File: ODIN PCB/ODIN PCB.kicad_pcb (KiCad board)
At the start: 2 copper layers, 67.6 x 56.4 mm, 18 parts, among them P2 POWER, SW1 BATTEST

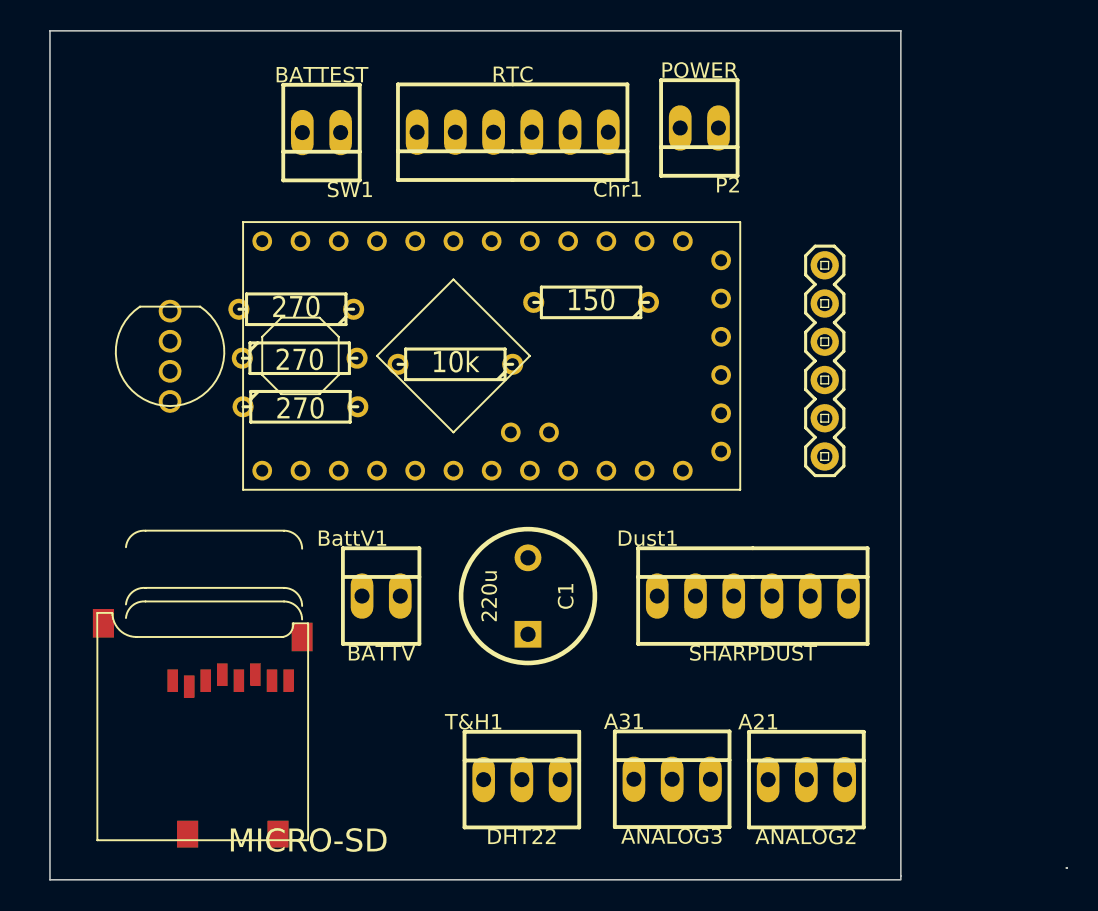
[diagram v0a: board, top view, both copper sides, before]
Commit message: Next iteration. Better net labelling. From Sam's message: "I've got it down to about 40mm x 56 mm.   Probably needs checking for connectivity issues and errors.   It passed the KiCad design rules check.   If we want to hang the SD card off the edge of the top surface the pin orientation does not need to be changed but I'd need to move the footprint to the left to avoid an overlap with the battery test header.   I haven't done anything with the silkscreen labels yet"
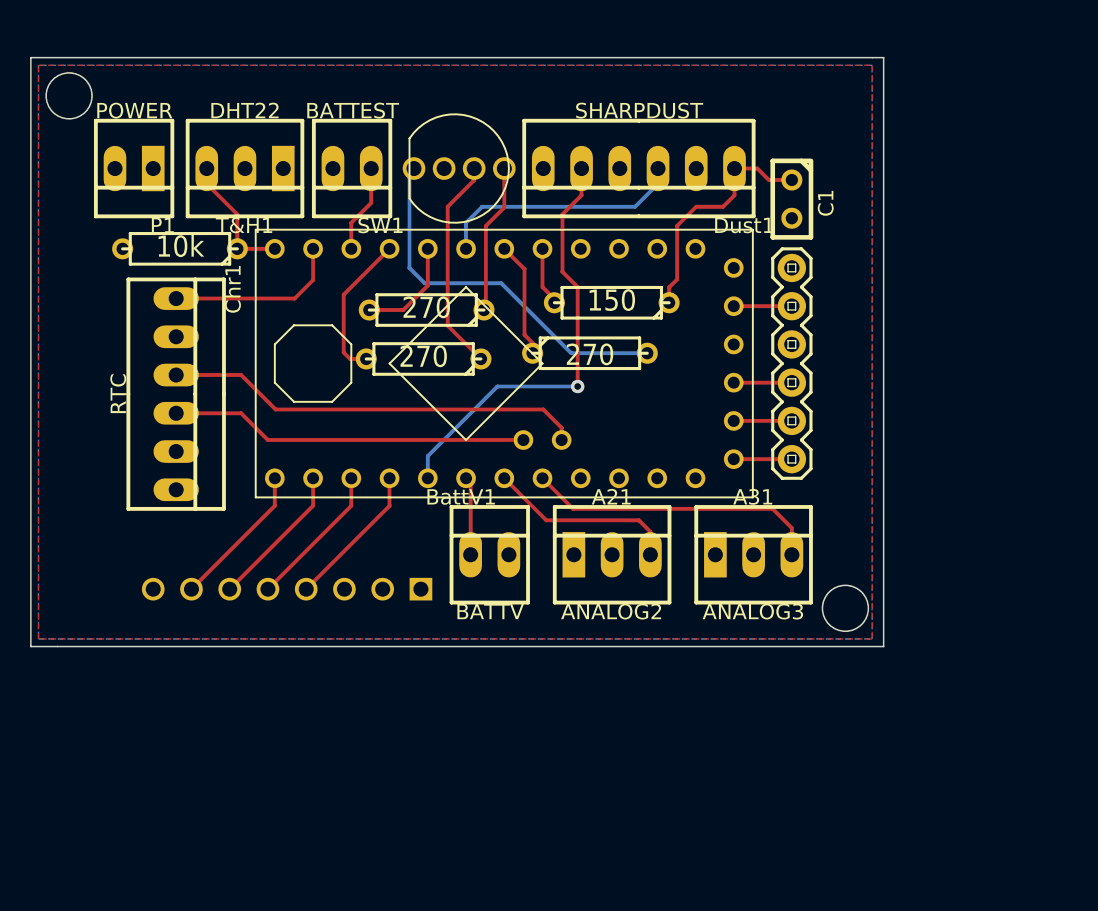
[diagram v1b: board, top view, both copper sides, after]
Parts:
- removed P2: POWER, PINHEAD1-2
- added P1: POWER, conn2pwr, F.Cu at (126.2, 106.9)
- A21, A31, T&H1: footprint PINHEAD1-3 -> header3
- C1: footprint C2V8 -> C1
- GUS1: value 5MMRGBLED -> 5mmRGB
- SD1: footprint adafruit-MICROSD -> microSD; moved to B.Cu
- moved T&H1 44.6 mm to (133.6, 106.9), turned to 180 degrees
- moved C1 31.7 mm to (169.9, 109.0), turned to 270 degrees
- moved Dust1 29.4 mm to (159.8, 106.9), turned to 180 degrees
- moved Chr1 28.3 mm to (129.0, 121.9), turned to 270 degrees
- moved GUS1 22.9 mm to (147.8, 106.9), turned to 0 degrees
- moved R1 19.8 mm to (129.3, 112.3)
- moved A21 19.7 mm to (158.0, 132.6)
- moved R2 19.7 mm to (156.5, 119.2), turned to 0 degrees
- moved SD1 16.9 mm to (135.1, 134.9)
- moved A31 15.9 mm to (167.4, 132.6)
- moved R3 10.6 mm to (145.7, 116.3), turned to 180 degrees
- moved R4 8.23 mm to (145.5, 119.6), turned to 180 degrees
- moved BattV1 7.72 mm to (149.9, 132.6)
- moved SW1 3.14 mm to (140.7, 106.9)
- moved JP1 2.19 mm to (169.9, 126.2)
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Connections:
- net N-0000010 renamed /D2
- net N-0000017 renamed /D7
- net N-0000023 renamed /DO
- net N-0000024 renamed /CLK
- net N-0000025 renamed /A3
- net N-0000028 renamed /DTR
- net N-0000029 renamed /CTS
- net N-0000030 renamed /SCL
- net N-0000031 renamed /A2
- net N-0000032 renamed /SQW
- net N-0000033 renamed /SDA
- net N-0000038 renamed /D3
- net N-0000039 renamed /D5
- net N-0000040 renamed /D1
- net N-0000041 renamed /D0
- net N-0000047 renamed /CS
- net N-0000048 renamed /DI
- net N-0000050 renamed /D4
- net N-000006 renamed /A1
- net N-000008 renamed /D6
- net N-000009 renamed /A0
- APM1 pad D9: N-0000044 -> /D9
- APM1 pad GND1: (no net) -> /GND
- APM1 pad VCC1: (no net) -> /VCC
- BattV1 pad 2: (no net) -> /GND
- C1 pad 2: N-0000027 -> /GND
- Chr1 pad 5: (no net) -> /VCC
- Chr1 pad 6: (no net) -> /GND
- Dust1 pad 2: N-0000027 -> /GND
- Dust1 pad 4: N-0000027 -> /GND
- Dust1 pad 6: (no net) -> /VCC
- GUS1 pad GND: (no net) -> /GND
- JP1 pad GND: (no net) -> /GND
- JP1 pad VCC: (no net) -> /VCC
- R1 pad 1: N-0000044 -> /D9
- R1 pad 2: N-0000045 -> /VCC
- SD1 pad 6: (no net) -> /GND
- SD1 pad 8: (no net) -> /VCC
- SW1 pad 2: (no net) -> /VCC
- T&H1 pad 3: N-0000045 -> /D9
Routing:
- net /A0: track 0.00 -> 28.8 mm, vias 0 -> 1
- net /SDA: track 0.00 -> 27.9 mm
- net N-0000013: track 0.00 -> 24.9 mm
- net /SCL: track 0.00 -> 23.8 mm
- net /A3: track 0.00 -> 19.7 mm
- net /D4: track 0.00 -> 16.6 mm
- net N-000001: track 0.00 -> 15.9 mm
- net N-0000015: track 0.00 -> 14.3 mm
- net /A2: track 0.00 -> 12.7 mm
- net /SQW: track 0.00 -> 11.7 mm
- net N-0000014: track 0.00 -> 9.96 mm
- net /D6: track 0.00 -> 9.82 mm
- net /DO: track 0.00 -> 9.66 mm
- net /DI: track 0.00 -> 9.66 mm
- net /CS: track 0.00 -> 9.66 mm
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- added copper zone on B.Cu, net /GND
- added copper zone on F.Cu, net /VCC
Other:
- board size 67.6 x 56.4 mm -> 56.6 x 39.1 mm

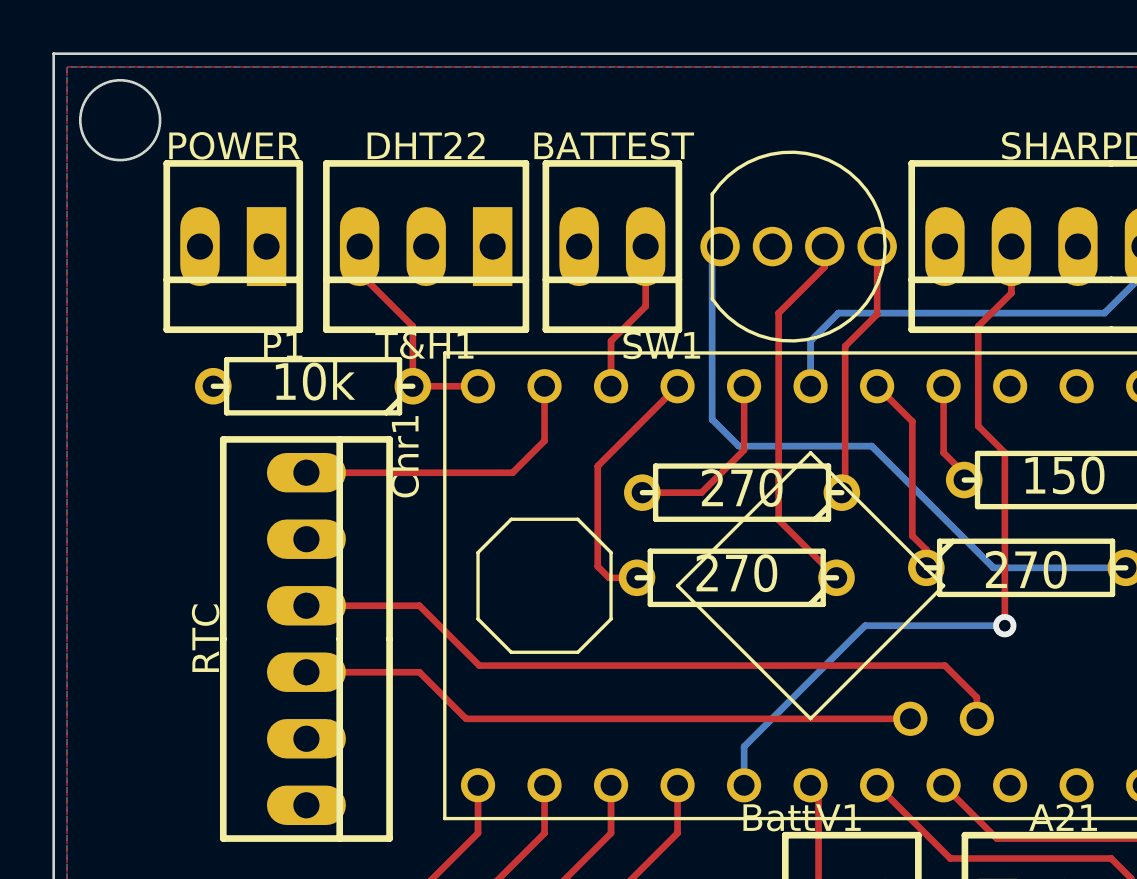
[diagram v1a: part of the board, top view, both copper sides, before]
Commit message: Swapped SDA/SCL pins, moved RTC alarm trigger to Arduino pin 2 interrupt. RGB led leg on pin 2 moved to pin 8. Libraries added as some parts within libraries modified.
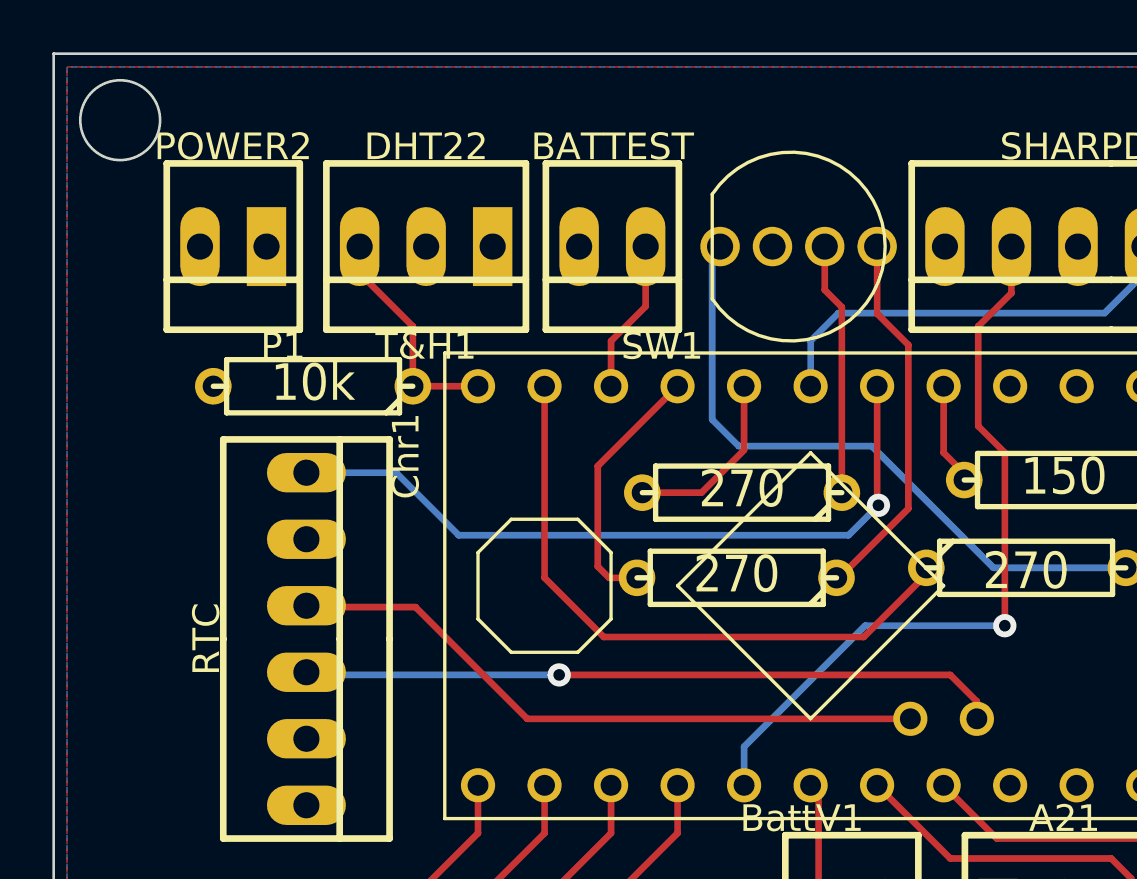
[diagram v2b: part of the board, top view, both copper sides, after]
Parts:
- GUS1: value 5mmRGB -> 5MMRGBLED
- P1: value POWER -> POWER2
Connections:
- APM1 pad A4: /SCL -> /SDA
- APM1 pad A5: /SDA -> /SCL
- APM1 pad D3: /D3 -> /SQW
- APM1 pad D8: /SQW -> /D8
- GUS1 pad BLU: N-0000015 -> N-000001
- GUS1 pad GRN: N-0000014 -> N-000006
- R2 pad 1: /D3 -> /D8
- R3 pad 1: N-0000014 -> N-000001
- R4 pad 1: N-0000015 -> N-000006
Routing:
- net /D8: track 0.00 -> 24.1 mm
- net /SQW: track 11.7 -> 27.9 mm, vias 0 -> 1
- net N-000006: track 0.00 -> 14.3 mm
- net N-0000015: track 14.3 -> 0.00 mm
- net N-0000014: track 9.96 -> 0.00 mm
- net N-000001: track 0.00 -> 9.67 mm
- net /D3: track 7.71 -> 0.00 mm
- net /SDA: track 27.9 -> 24.9 mm
- net /SCL: track 23.8 -> 26.8 mm, vias 0 -> 1
